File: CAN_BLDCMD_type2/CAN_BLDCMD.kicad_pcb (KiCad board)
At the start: 2 copper layers, 70 x 90 mm, 213 parts, among them J1 SWD, J10 BATT_IN, J11 OUT_U, J12 OUT_V, J13 OUT_W, J14 VALVE, J15 HALL_IN, J2 CAN, J3 CAN, J4 ENC, J5 I/O0, J6 I/O1, J7 SERIAL, J8 FAN, J9 BATT_IN, Q1 MOSFET_N, Q2 MOSFET_N, Q3 MOSFET_N, Q4 MOSFET_N, Q5 MOSFET_N, Q6 MOSFET_N, Q7 NPN, Q8 NPN, SW1 SW0, SW2 SW1, SW3 RST, SW4 MODE, U1 MAX3051, U10 SI8900, U11 ADC_~RST, U12 ACS758, U13 ACS758, U14 ACS758, U15 BD9G101G, U16 LTC2644, U17 LTC2644, U18 BD33FA1, U19 LOGO, U2 BD9G101G, U20 AQM0802, U3 STM32F405RG, U4 AZ1086H, U5 ADRESS, U6 POWER_ON, U7 SI8274, U8 SI8274, U9 SI8274, Y1 8MHz

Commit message: MAIN基板，大体の構成完了．あとは配線を少し修正するのみ
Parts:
- removed C31, C32: 470n, Capacitor_SMD:C_0603_1608Metric
- removed C34, C35: 0.1u, Capacitor_SMD:C_0603_1608Metric
- removed R30, R31: 4.7k, Mizz_lib:1608_WP
- removed U13, U14: ACS758, Mizz_lib:ACS785xCB
- moved U12 91.2 mm to (277.5, 106.0)
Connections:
- Q2 pad S: Net-(Q2-PadS) -> /H_BridgeOut
- Q4 pad S: Net-(Q4-PadS) -> /H_BridgeOut
- Q6 pad S: Net-(Q6-PadS) -> /H_BridgeOut
- U12 pad 4: Net-(Q2-PadS) -> /H_BridgeOut
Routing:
- net Net-(Q6-PadS): vias 10 -> 0
- net Net-(Q4-PadS): vias 10 -> 0
- net Net-(Q2-PadS): vias 10 -> 0
- net /H_BridgeOut: vias 0 -> 30
- added copper zone on B.Cu, net /H_BridgeOut
- added copper zone on F.Cu, net /H_BridgeOut
- removed copper zone on B.Cu, net Net-(Q2-PadS)
- removed copper zone on F.Cu, net Net-(Q2-PadS)
- removed copper zone on B.Cu, net Net-(Q4-PadS)
- removed copper zone on B.Cu, net Net-(Q6-PadS)

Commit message: 肩痛い
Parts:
- removed C44, C45, C46, C51, C52, C53, C54: 0.1u, Capacitor_SMD:C_0603_1608Metric
- removed R51, R53: 1k, Mizz_lib:1608_WP
- removed R52: 10k, Mizz_lib:1608_WP
- removed U16, U17: LTC2644, Package_SO:MSOP-12_3x4mm_P0.65mm
- removed U18: BD33FA1, Package_TO_SOT_SMD:SOT-89-3
- added C31: 0.1u, Capacitor_SMD:C_0603_1608Metric, F.Cu at (161.7, 15.8)
- added C32: 0.1u, Capacitor_SMD:C_0603_1608Metric, F.Cu at (165.7, 15.8)
- added C34: 0.1u, Capacitor_SMD:C_0603_1608Metric, F.Cu at (179.1, 6.95)
- added D28: LED, LED_SMD:LED_0603_1608Metric, F.Cu at (179.1, 4.40)
- added ISO1: Si8660BA, Package_SO:SOIC-16_3.9x9.9mm_P1.27mm, F.Cu at (223.3, 103.8)
- added R30: 100k, Mizz_lib:1608_WP, F.Cu at (204.3, 79.6)
- added R31: 100k, Mizz_lib:1608_WP, F.Cu at (216.7, 79.6)
- C12, C56, C8, D14, D15, D16, R36, R38, R45, R46, U2, U4: moved to B.Cu
- R28: value 4.7k -> 100k
- R32: value 4.7k -> 20k; moved to B.Cu
- R48, R50: value 10k -> 100
- R49: value 1k -> 100
- R64: value 510 -> 1k
- U10: value SI8900 -> LM324; footprint Package_SO:SOIC-16W_7.5x10.3mm_P1.27mm -> Package_SO:TSSOP-14_4.4x5mm_P0.65mm
- U11: value ADC_~RST -> NJM78L05; footprint Package_SO:SOIC-4_4.55x2.6mm_P1.27mm -> Package_TO_SOT_SMD:SOT-89-3; moved to F.Cu
- moved R32 186.1 mm to (239.1, 98.0), turned to 270 degrees
- moved D14 155.4 mm to (237.6, 93.6), turned to 90 degrees
- moved C8 153.8 mm to (193.8, 121.8)
- moved C58 149.4 mm to (238.7, 103.3), turned to 90 degrees
- moved L2 138.7 mm to (239.9, 95.8), turned to 270 degrees
- moved C60 124.4 mm to (229.1, 95.8), turned to 90 degrees
- moved C42 118.6 mm to (226.9, 99.3), turned to 180 degrees
- moved D16 118.3 mm to (241.7, 96.3), turned to 90 degrees
- moved C59 114.7 mm to (235.2, 99.6), turned to 90 degrees
- moved C56 113.7 mm to (241.7, 92.2), turned to 90 degrees
- moved R35 111.6 mm to (202.8, 79.6), turned to 270 degrees
- moved R37 107.9 mm to (215.2, 79.6), turned to 270 degrees
- moved R50 105.0 mm to (180.3, 15.2)
- moved R46 103.8 mm to (232.3, 101.2), turned to 180 degrees
- moved U2 103.4 mm to (193.7, 124.3), turned to 180 degrees
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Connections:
- net /H_BridgeOut renamed /INVERTER_OUT
- net /OUT_U_Current renamed /Current
- net /OUT_V_Current renamed Net-(U3-Pad26)
- net /OUT_W_Current renamed Net-(U3-Pad27)
- C42 pad 1: +3.3VP -> +5VP
- C60 pad 1: +3.3VP -> +5VP
- R27 pad 1: Net-(R27-Pad1) -> /LED2
- R27 pad 2: GND -> Net-(D28-Pad2)
- R28 pad 1: +3.3VP -> /OUT_U
- R28 pad 2: Net-(R28-Pad2) -> /ZERO_CROSS
- R48 pad 1: /OUT_U -> Net-(C31-Pad1)
- R48 pad 2: /OUT_U_DIGITAL<3V3P -> /OUT_U
- R49 pad 1: /OUT_U_DIGITAL<3V3P -> Net-(C32-Pad1)
- R49 pad 2: GNDPWR -> /OUT_V
- R50 pad 1: /OUT_V -> Net-(C34-Pad1)
- R50 pad 2: /OUT_V_DIGITAL<3V3P -> /OUT_W
- R64 pad 2: +3.3VP -> +5VP
- U10 pad 1: +3.3VP -> /SIGNAL_V
- U10 pad 10: +3V3 -> /OUT_W
- U10 pad 11: Net-(U10-Pad11) -> GNDPWR
- U10 pad 12: /USARTx_RX -> Net-(U10-Pad12)
- U10 pad 13: /USARTx_TX -> Net-(U10-Pad13)
- U10 pad 2: +3.3VP -> /ZERO_CROSS
- U10 pad 3: /OUT_U_Analog -> /OUT_V
- U10 pad 4: /OUT_V_Analog -> +BATT
- U10 pad 5: /OUT_W_Analog -> /OUT_U
- U10 pad 6: Net-(U10-Pad6) -> /ZERO_CROSS
- U10 pad 7: Net-(R28-Pad2) -> /SIGNAL_U
- U10 pad 8: GNDPWR -> /SIGNAL_W
- U10 pad 9: GND -> /ZERO_CROSS
- U11 pad 1: /ADC_~RST~_Pin -> +12P
- U11 pad 2: Net-(R27-Pad1) -> GNDPWR
- U11 pad 3: GNDPWR -> +5VP
- U3 pad 11: Net-(U3-Pad11) -> /LED2
- U3 pad 14: /PWR_ON_Pin -> /LOCATION_U_SIGNAL
- U3 pad 15: /ADC_~RST~_Pin -> /LOCATION_V_SIGNAL
- U3 pad 16: /USARTx_TX -> /LOCATION_W_SIGNAL
- U3 pad 17: /USARTx_RX -> /PWR_ON_Pin
- U3 pad 29: /ADRESS_0 -> /I2Cx_SCL
- U3 pad 30: /ADRESS_1 -> /I2Cx_SDA
- U3 pad 33: /ADRESS_2 -> Net-(U3-Pad33)
- U3 pad 34: /ADRESS_3 -> Net-(U3-Pad34)
- U3 pad 38: Net-(U3-Pad38) -> /ADRESS_0
- U3 pad 39: Net-(U3-Pad39) -> /ADRESS_1
- U3 pad 40: Net-(U3-Pad40) -> /ADRESS_2
- U3 pad 41: Net-(U3-Pad41) -> /ADRESS_3
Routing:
- net Net-(R33-Pad2): track 22.7 -> 0.00 mm
- net /SIGNAL_V: track 0.00 -> 22.3 mm
- net /Drive_U_Temp: track 21.1 -> 0.00 mm, vias 3 -> 0
- net +Batt: track 0.00 -> 19.3 mm, vias 0 -> 1
- net /SIGNAL_U: track 0.00 -> 18.3 mm
- net GNDPWR: track 20.2 -> 2.37 mm
- net +BATT: track 10.7 -> 27.9 mm, vias 102 -> 103
- net Net-(R34-Pad2): track 17.0 -> 0.00 mm, vias 1 -> 0
- net /SIGNAL_W: track 0.00 -> 16.5 mm
- net +12P: track 0.00 -> 15.7 mm
- net /FB_12P: track 0.00 -> 12.8 mm, vias 0 -> 2
- net /OUT_U: track 19.7 -> 7.10 mm, vias 40 -> 41
- net +5VP: track 0.00 -> 9.64 mm
- net Net-(C47-Pad1): track 0.00 -> 8.36 mm, vias 0 -> 1
- net Net-(Q1-PadG): track 7.80 -> 0.00 mm, vias 1 -> 0
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- removed copper zone on F.Cu, net /INVERTER_OUT
- removed copper zone on F.Cu, net Net-(Q4-PadS)
- removed copper zone on F.Cu, net Net-(Q6-PadS)
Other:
- outline, holes or cut-outs redrawn
- board text added: "Brushless DC-Motor Driver Type-2 ver.0.0 Gemini Castor."
- board text removed: "Brushless DC-Motor Driver Type-0 ver.0.0 Virgo Spica."

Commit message: BLDC type2引き終わった，基板にミスがあった
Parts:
- added C35: 0.1u, Mizz_lib:1608_WP, F.Cu at (219.9, 80.3)
- added C44: 0.1u, Mizz_lib:1608_WP, B.Cu at (192.4, 107.2)
- added C45: 0.1u, Mizz_lib:1608_WP, B.Cu at (204.7, 107.2)
- added C46: 0.1u, Mizz_lib:1608_WP, B.Cu at (216.9, 107.2)
- C10, C18, C19, C21, C3, C33, C4, C43, C61, C62, C63, C64, C9, D1, D7, JP1, R1, R10, R11, R12, R15, R16, R17, R18, R19, R2, R22, R25, R26, R29, R3, R54, R55, R65, R7: moved to B.Cu
- C11, C17, C28, C6: footprint Capacitor_SMD:C_0603_1608Metric -> Mizz_lib:1608_WP
- C13, C15, C16, C20, C22, C23, C24, C25, C26, C27, C29, C30, C5, C7: footprint Capacitor_SMD:C_0603_1608Metric -> Mizz_lib:1608_WP; moved to B.Cu
- D27: value 3V3P -> 5VP
- D28: value LED -> EMG
- D5: value LED -> MODE
- D6: value LED -> BUS
- R20, R21: value 100k -> 10k; moved to B.Cu
- R23, R24: value 10k -> 100k; moved to B.Cu
- moved C7 162.5 mm to (219.0, 120.5), turned to 315 degrees
- moved JP3 159.4 mm to (234.9, 142.0), turned to 180 degrees
- moved D6 158.1 mm to (191.2, 113.2)
- moved C5 143.7 mm to (207.8, 121.2), turned to 225 degrees
- moved D7 139.5 mm to (232.4, 139.0), turned to 270 degrees
- moved C43 139.3 mm to (235.2, 102.4)
- moved C4 131.2 mm to (198.5, 124.3), turned to 270 degrees
- moved C6 130.6 mm to (213.1, 127.6)
- moved R7 130.5 mm to (240.9, 115.2), turned to 180 degrees
- moved JP1 129.0 mm to (232.9, 127.2), turned to 180 degrees
- moved C2 127.7 mm to (201.0, 111.9), turned to 45 degrees
- moved C33 121.4 mm to (225.7, 110.8)
- moved R5 120.5 mm to (230.3, 131.8), turned to 90 degrees
- moved C9 120.1 mm to (180.6, 116.8), turned to 90 degrees
- moved D1 119.8 mm to (231.5, 123.3), turned to 270 degrees
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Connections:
- C10 pad 1: +12V -> CAN_Vdd
- C12 pad 1: Net-(C12-Pad1) -> +12V
- C14 pad 1: Net-(C12-Pad1) -> +12V
- C9 pad 1: +12V -> CAN_Vdd
- D3 pad 1: Net-(C12-Pad1) -> +12V
- D3 pad 2: +12V -> CAN_Vdd
- J2 pad 2: +12V -> CAN_Vdd
- J3 pad 2: +12V -> CAN_Vdd
- U2 pad 4: Net-(C12-Pad1) -> +12V
- U2 pad 5: Net-(C12-Pad1) -> +12V
- U3 pad 14: /LOCATION_U_SIGNAL -> /PWM_V
- U3 pad 15: /LOCATION_V_SIGNAL -> /PWM_W
- U3 pad 16: /LOCATION_W_SIGNAL -> /Enable
- U3 pad 17: /PWR_ON_Pin -> /PWM_U
- U3 pad 2: /SW0 -> /LOCATION_W_SIGNAL
- U3 pad 20: /Drive_U_Temp -> /Drive_W_Temp
- U3 pad 22: /Drive_W_Temp -> /Drive_U_Temp
- U3 pad 26: Net-(U3-Pad26) -> /VALVE_0
- U3 pad 27: Net-(U3-Pad27) -> /VALVE_1
- U3 pad 3: /SW1 -> /LOCATION_V_SIGNAL
- U3 pad 37: /SW_MODE -> Net-(U3-Pad37)
- U3 pad 38: /ADRESS_0 -> Net-(U3-Pad38)
- U3 pad 39: /ADRESS_1 -> Net-(U3-Pad39)
- U3 pad 4: Net-(U3-Pad4) -> /LOCATION_U_SIGNAL
- U3 pad 40: /ADRESS_2 -> /ADRESS_1
- U3 pad 41: /ADRESS_3 -> /ADRESS_0
- U3 pad 44: Net-(U3-Pad44) -> /ADRESS_3
- U3 pad 45: Net-(U3-Pad45) -> /ADRESS_2
- U3 pad 54: Net-(U3-Pad54) -> /SW0
- U3 pad 55: Net-(U3-Pad55) -> /SW1
- U3 pad 58: Net-(U3-Pad58) -> /PWR_ON_Pin
- U3 pad 59: Net-(U3-Pad59) -> /SW_MODE
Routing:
- net +3V3: track 0.00 -> 311.1 mm, vias 0 -> 21
- net +5V: track 0.00 -> 104.7 mm, vias 0 -> 4
- net /Drive_U_Temp: track 0.00 -> 73.7 mm, vias 0 -> 2
- net /Drive_V_Temp: track 0.00 -> 66.1 mm, vias 0 -> 4
- net +12P: track 15.7 -> 80.2 mm, vias 0 -> 7
- net /OUT_U: track 7.10 -> 70.6 mm, vias 41 -> 43
- net /Enable: track 0.00 -> 57.7 mm, vias 0 -> 4
- net /~RST: track 0.00 -> 57.4 mm, vias 0 -> 5
- net /Drive_W_Temp: track 0.00 -> 52.0 mm, vias 0 -> 4
- net /ZERO_CROSS: track 0.00 -> 49.5 mm, vias 0 -> 5
- net /OUT_V: track 4.53 -> 51.1 mm, vias 41 -> 45
- net /OUT_W: track 4.82 -> 51.3 mm, vias 41 -> 39
- net +BATT: track 27.9 -> 63.3 mm, vias 103 -> 105
- net /CAN1_RX: track 0.00 -> 34.4 mm, vias 0 -> 3
- net /CAN_L: track 0.00 -> 34.4 mm, vias 0 -> 1
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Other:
- board text added: "-"
- board text added: "12V"
- board text added: "3.3V"
- board text added: "3V3"
- board text added: "5V"
- board text added: "A"
- board text added: "B"
- board text added: "CLK"
- board text added: "DIO"
- board text added: "Designed by A.Mizuta in 2020/03/10."
- board text added: "GND"
- board text added: "H"
- board text added: "HALL0"
- board text added: "HALL1"
- board text added: "HALL2"
- board text added: "I/O"
- board text added: "L"
- board text added: "NC"
- board text added: "Vdd"
- board text added: "~RST"
- board text added: "→3.3V"
- board text added: "▼"

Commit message: CAN BLDCMD type1完成したが，とても強引
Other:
- board text added: "RX"
- board text added: "TX"
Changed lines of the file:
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@@
   (general
     (thickness 1.6)
-    (drawings 70)
+    (drawings 74)
     (tracks 1783)
     (zones 0)
@@
   )
   (setup
-    (last_trace_width 0.5)
+    (last_trace_width 0.25)
     (user_trace_width 0.2)
     (user_trace_width 0.3)
@@
       (drillshape 0)
       (scaleselection 1)
-      (outputdirectory "C:/Users/3Zuta/Documents/NHK_RC20_PCBs/CAN_BLDCMD_type2/加工ファイル/"))
+      (outputdirectory "加工ファイル/"))
   )
   (net 0 "")
@@
     )
   )
+  (gr_text RX (at 225.1 126.4) (layer B.SilkS)
+    (effects (font (size 0.8 0.8) (thickness 0.15)) (justify mirror))
+  )
+  (gr_text TX (at 225.1 123.85) (layer B.SilkS)
+    (effects (font (size 0.8 0.8) (thickness 0.15)) (justify mirror))
+  )
+  (gr_text 5V (at 225.1 121.4) (layer B.SilkS)
+    (effects (font (size 0.8 0.8) (thickness 0.15)) (justify mirror))
+  )
+  (gr_text GND (at 225.1 118.85) (layer B.SilkS)
+    (effects (font (size 0.8 0.8) (thickness 0.15)) (justify mirror))
+  )
   (gr_text NC (at 228.65 113.3 90) (layer B.SilkS)

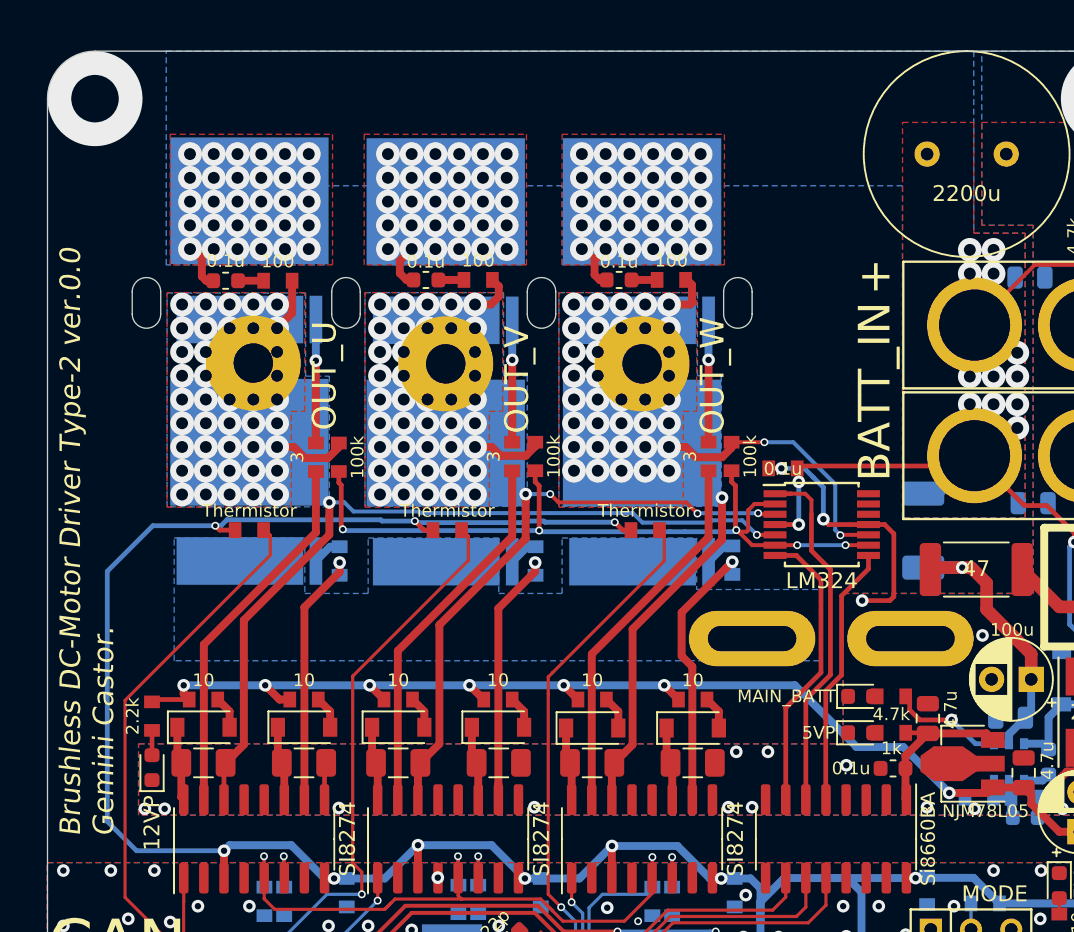
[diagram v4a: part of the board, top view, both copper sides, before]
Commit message: BLDCMD type2,ロータ位置推定回路修正
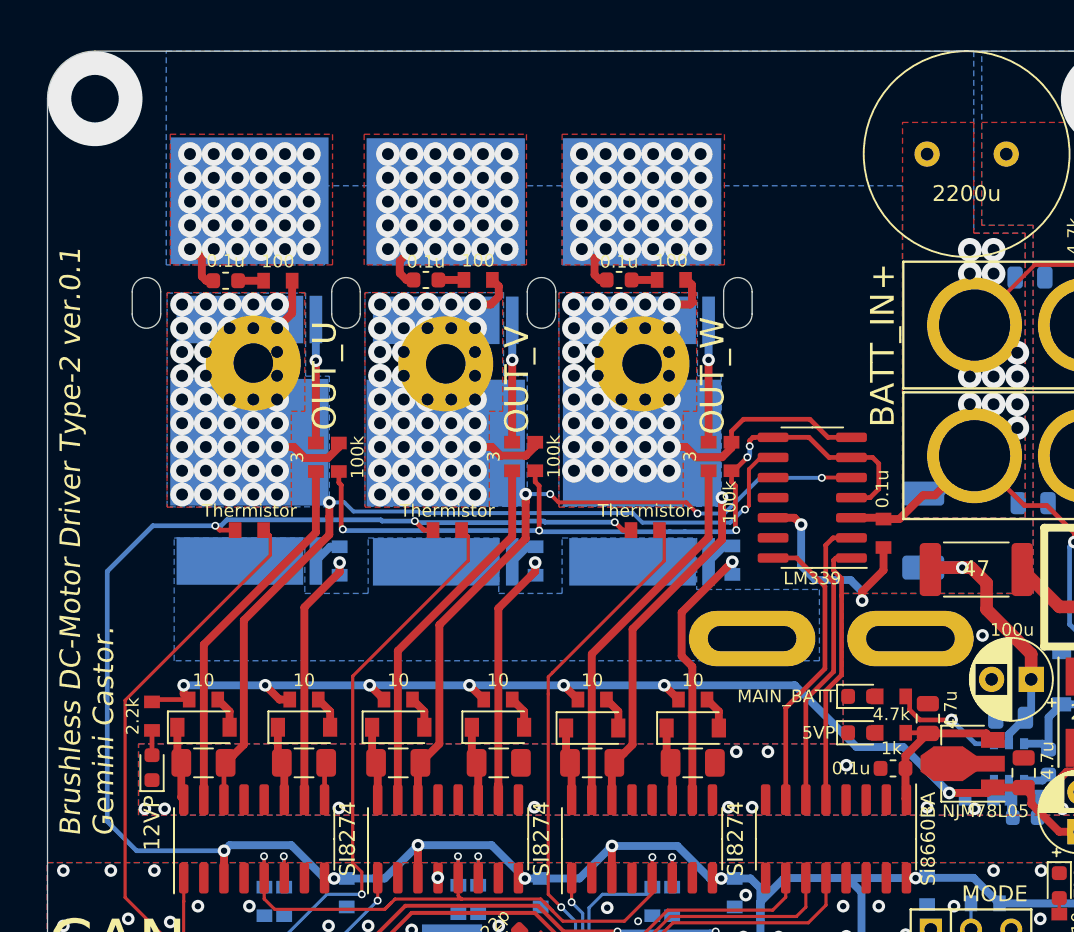
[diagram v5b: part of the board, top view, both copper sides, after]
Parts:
- U10: value LM324 -> LM339; footprint Package_SO:TSSOP-14_4.4x5mm_P0.65mm -> Package_SO:SOIC-14_3.9x8.7mm_P1.27mm
- moved C35 7.56 mm to (226.3, 84.5), turned to 270 degrees
- moved U10 1.80 mm to (221.8, 82.2), turned to 180 degrees
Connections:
- U10 pad 1: /SIGNAL_V -> /SIGNAL_W
- U10 pad 10: /OUT_W -> Net-(U10-Pad10)
- U10 pad 11: GNDPWR -> Net-(U10-Pad11)
- U10 pad 12: Net-(U10-Pad12) -> GNDPWR
- U10 pad 14: Net-(U10-Pad14) -> /SIGNAL_U
- U10 pad 2: /ZERO_CROSS -> /SIGNAL_V
- U10 pad 3: /OUT_V -> +BATT
- U10 pad 4: +BATT -> /ZERO_CROSS
- U10 pad 5: /OUT_U -> /OUT_V
- U10 pad 7: /SIGNAL_U -> /OUT_W
- U10 pad 8: /SIGNAL_W -> /ZERO_CROSS
- U10 pad 9: /ZERO_CROSS -> /OUT_U
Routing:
- net +BATT: track 63.3 -> 56.1 mm, vias 105 -> 103
- net /OUT_V: track 51.1 -> 56.9 mm
- net /OUT_W: track 51.3 -> 47.5 mm, vias 39 -> 37
- net GNDPWR: track 19.2 -> 15.9 mm, vias 33 -> 32
- net /OUT_U: track 70.6 -> 73.1 mm
- net /SIGNAL_V: track 22.5 -> 20.1 mm
- net /ZERO_CROSS: track 49.5 -> 51.3 mm
- net /SIGNAL_W: track 16.5 -> 17.6 mm
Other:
- board text added: "Brushless DC-Motor Driver Type-2 ver.0.1 Gemini Castor."
- board text added: "Designed by A.Mizuta in 2020/04/13."
- board text removed: "Brushless DC-Motor Driver Type-2 ver.0.0 Gemini Castor."
- board text removed: "Designed by A.Mizuta in 2020/03/10."
